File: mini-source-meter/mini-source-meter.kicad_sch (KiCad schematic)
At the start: 32 parts, among them IC1 ADA4351-2ACPZ-R7, J1 Conn_01x01_Pin, J2 Conn_01x01_Pin, J3 Conn_01x01_Pin, J4 Conn_01x01_Pin, J5 Conn_01x01_Pin, U1 OPA992, U2 OPA992, U3 MCP4725xxx-xCH, U4 MCP4725xxx-xCH

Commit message: fixed DAC power rails in schmatic
place and routed components on layout
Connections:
- net +5VA: now also U3.3 (VDD), U4.3 (VDD); no longer U3.2 (VSS), U4.2 (VSS)
- net GND: now also U3.2 (VSS), U4.2 (VSS); no longer U3.3 (VDD), U4.3 (VDD)
- net IoutB: now also C2.1
- net at IC1.7 (OUTB), R5.2: no longer C2.1
- net at R2.1, R9.1: now also IC1.15 (SW1_A); no longer IC1.16 (SW0_A)
- net at R1.2: now also IC1.16 (SW0_A); no longer IC1.15 (SW1_A)
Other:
- moved on the sheet: C2, R1, R2, R9

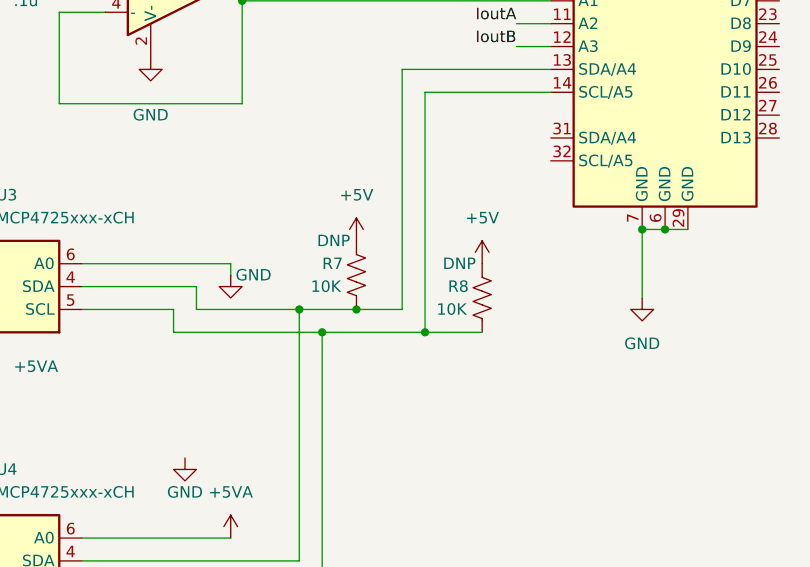
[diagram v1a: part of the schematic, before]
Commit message: moved a trace
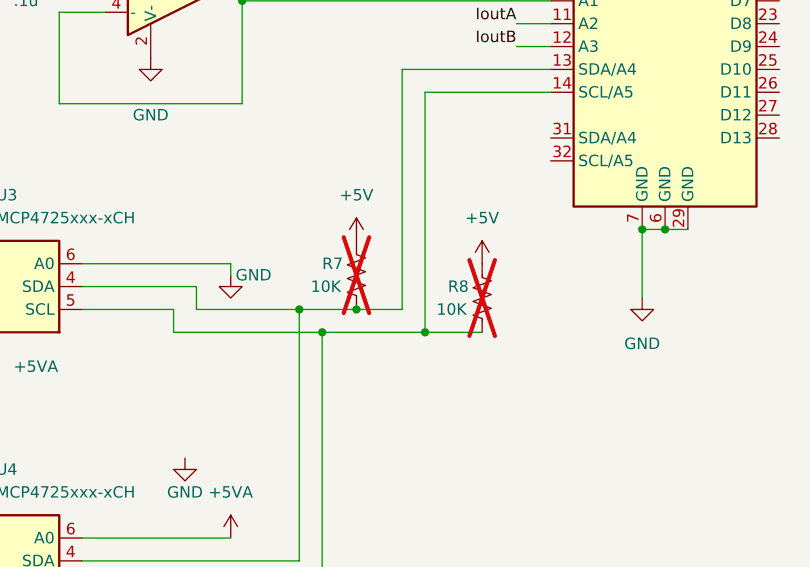
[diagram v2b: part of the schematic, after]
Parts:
- R7, R8: DNP DNP -> (none); now not fitted
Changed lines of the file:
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@@
   )
   (symbol (lib_id "Device:R_US") (at 172.72 110.49 180) (unit 1)
-    (in_bom yes) (on_board yes) (dnp no)
+    (in_bom yes) (on_board yes) (dnp yes)
     (property "Reference" "R7" (at 168.91 109.22 0)
       (effects (font (size 1.27 1.27)) (justify right))
@@
       (effects (font (size 1.27 1.27)) hide)
     )
-    (property "Datasheet" "~" (at 172.72 110.49 0)
-      (effects (font (size 1.27 1.27)) hide)
-    )
-    (property "DNP" "DNP" (at 170.18 106.68 0)
-      (effects (font (size 1.27 1.27)))
+    (property "Datasheet" "~" (at 172.72 110.49 0) (show_name)
+      (effects (font (size 1.27 1.27)) hide)
     )
     (pin "1")
@@
   )
   (symbol (lib_id "Device:R_US") (at 186.69 113.03 180) (unit 1)
-    (in_bom yes) (on_board yes) (dnp no)
+    (in_bom yes) (on_board yes) (dnp yes)
     (property "Reference" "R8" (at 182.88 111.76 0)
       (effects (font (size 1.27 1.27)) (justify right))
@@
       (effects (font (size 1.27 1.27)) hide)
     )
-    (property "DNP" "DNP" (at 184.15 109.22 0)
-      (effects (font (size 1.27 1.27)))
-    )
-    (pin "1")
+    (pin "1")
